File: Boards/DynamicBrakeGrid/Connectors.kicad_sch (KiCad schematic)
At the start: 48 parts, among them J1 1987724, J10 5442251, J11 5442251, J12 5442251, J13 38969-0002, J14 5442251, J15 5442251, J16 1548129, J17 1548129, J2 1987724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

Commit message: Update Dynamic Brake Board
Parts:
- removed C1, C10: 100nF, symbol Device:C
- removed J16, J17, J22, J23: 1548129, InverterCom:1548129, symbol InverterCom:1548129
- added H10, H9: MountingHole_Pad, MountingHole:MountingHole_5.3mm_M5_ISO7380_Pad, symbol Mechanical:MountingHole_Pad
- added J18, J19, J20, J21, J22: 38969-0002, InverterCom:389690002, symbol InverterCom:38969-0002
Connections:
- net DC_LINK_V+: now also J18.1, J19.1, J20.1, J21.1, J22.1
- net GNDPWR: now also J18.2
- net RESISTOR_RETURN: now also J19.2, J20.2, J21.2, J22.2
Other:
- note removed: "SNUBBER CAPACITORS, PLACE HERE"

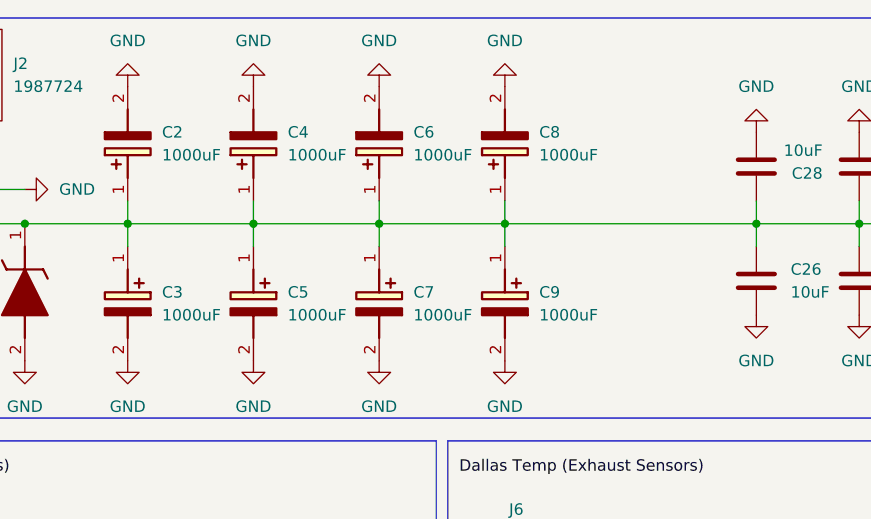
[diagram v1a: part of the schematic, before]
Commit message: Generate Bill of Materials
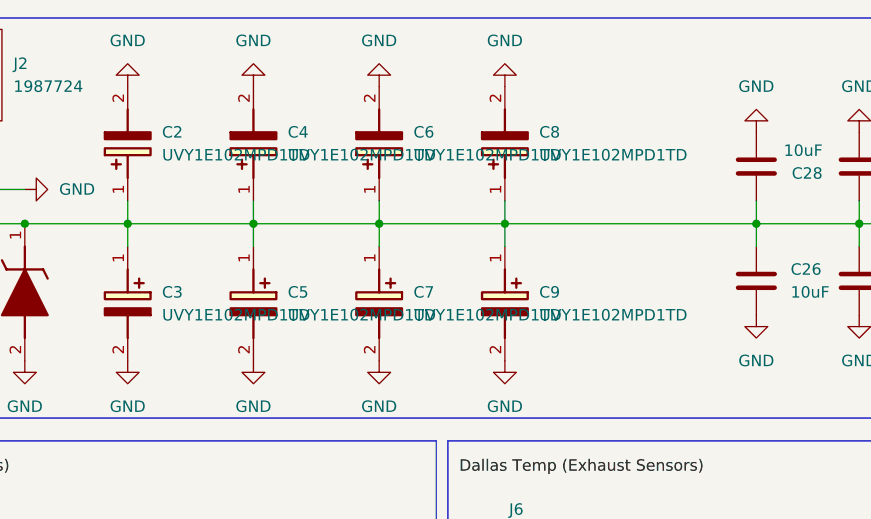
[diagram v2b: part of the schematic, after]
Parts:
- C2, C3, C4, C5, C6, C7, C8, C9: value 1000uF -> UVY1E102MPD1TD
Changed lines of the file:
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@@
 			)
 		)
-		(property "Value" "1000uF"
+		(property "Value" "UVY1E102MPD1TD"
 			(at 73.66 46.9899 90)
 			(effects
@@
 			)
 		)
-		(property "Value" "1000uF"
+		(property "Value" "UVY1E102MPD1TD"
 			(at 87.63 46.9899 90)
 			(effects
@@
 			)
 		)
-		(property "Value" "1000uF"
+		(property "Value" "UVY1E102MPD1TD"
 			(at 101.6 46.9899 90)
 			(effects
@@
 			)
 		)
-		(property "Value" "1000uF"
+		(property "Value" "UVY1E102MPD1TD"
 			(at 73.66 29.2099 90)
 			(effects
@@
 			)
 		)
-		(property "Value" "1000uF"
+		(property "Value" "UVY1E102MPD1TD"
 			(at 59.69 46.9899 90)
 			(effects
@@
 			)
 		)
-		(property "Value" "1000uF"
+		(property "Value" "UVY1E102MPD1TD"
 			(at 87.63 29.2099 90)
 			(effects
@@
 			)
 		)
-		(property "Value" "1000uF"
+		(property "Value" "UVY1E102MPD1TD"
 			(at 59.69 29.2099 90)
 			(effects
@@
 			)
 		)
-		(property "Value" "1000uF"
+		(property "Value" "UVY1E102MPD1TD"
 			(at 101.6 29.2099 90)
 			(effects
